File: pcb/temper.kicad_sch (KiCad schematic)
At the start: 0 parts

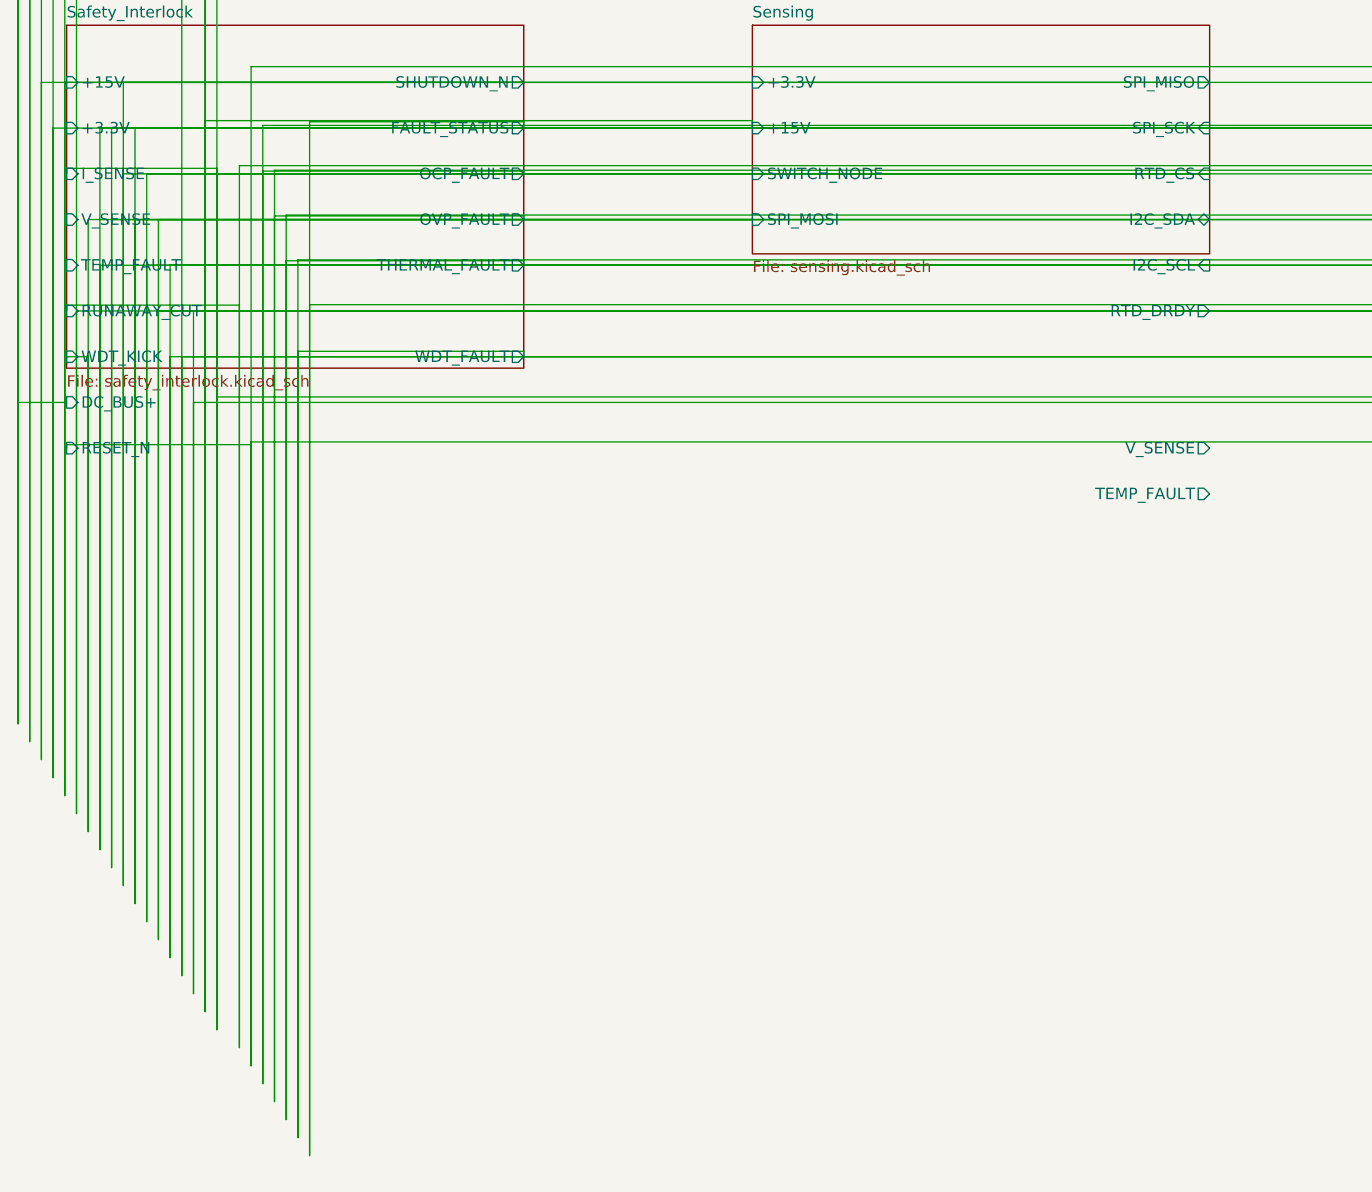
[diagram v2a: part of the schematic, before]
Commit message: fix: close root-vs-child pin reconciliation gaps (NTC_SENSE, stale V_SENSE/TEMP_FAULT/SWITCH_NODE)
Running the full root-vs-child sheet-pin reconciliation the plan promised
but hadn't actually executed found three more instances of the same defect
class the plan was closing out:

- Safety_Interlock's root symbol had V_SENSE/TEMP_FAULT input pins with no
  matching child-side hierarchical label (stale, same class as MCU_ENABLE).
- Safety_Interlock's child sheet declares a real NTC_SENSE input (feeds
  ThermalComparator.ntc_sense directly into the comparator) with no root
  pin at all -- unreachable from outside the sheet. Traced the intended
  source to Sensing, whose own NTC_SENSE producer fed an incomplete
  divider: the pull-up resistor was real, but the actual NTC thermistor
  (NCU18XH103F6SRB, IGBT case temp) was only ever a text annotation, never
  a placed component. Sensing's own V_SENSE/TEMP_FAULT output pins turned
  out to be equally vestigial (no consumer anywhere, never wired) and were
  removed too.
- Sensing's root symbol had a stale SWITCH_NODE input pin with no matching
  child-side label (Half_Bridge has the sheet's one legitimate instance).

Placed the real NTC thermistor and completed its divider in
sensing.kicad_sch, removed all four stale pins, and wired the two missing
NTC_SENSE root pins end to end. Verified via union-find including the full
divider chain and the root-level net.

Co-Authored-By: Claude Sonnet 5 <noreply@anthropic.com>
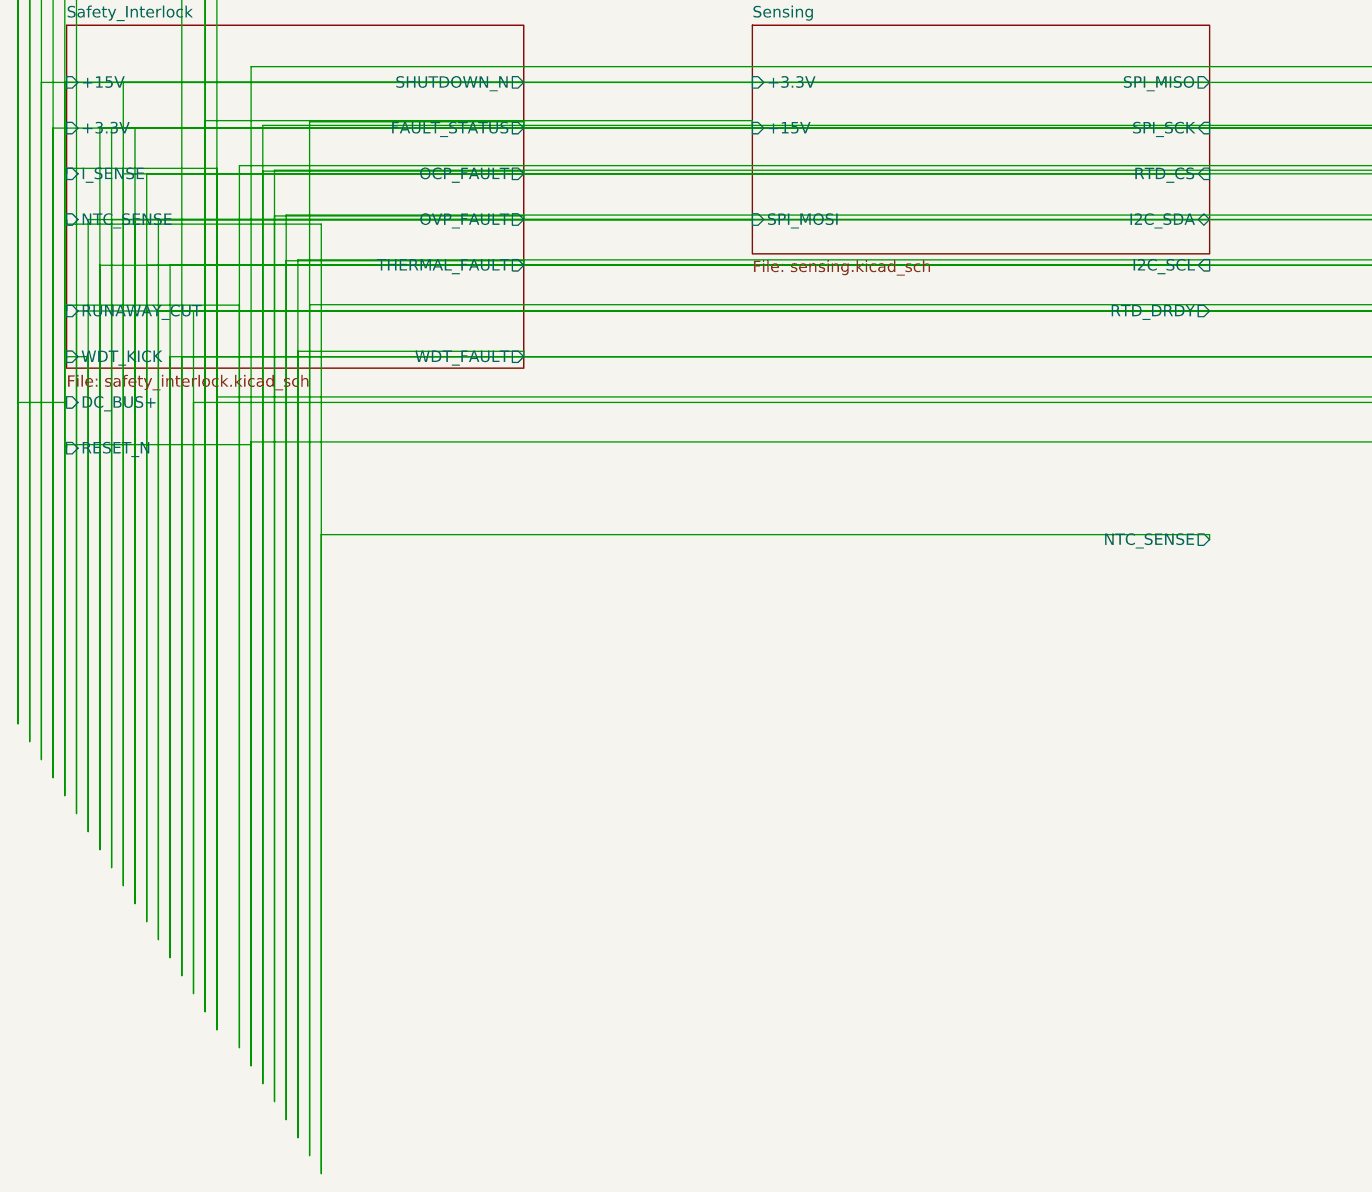
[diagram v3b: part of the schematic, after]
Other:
- sheet Safety_Interlock ports: added NTC_SENSE; removed TEMP_FAULT, V_SENSE
- sheet Sensing ports: added NTC_SENSE; removed SWITCH_NODE, TEMP_FAULT, V_SENSE
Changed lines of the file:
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@@
       )
     )
-    (pin "V_SENSE" input
+    (pin "NTC_SENSE" input
       (at 25.4 173.99 180)
-      (effects
-        (font
-          (size 1.27 1.27)
-        )
-        (justify left)
-      )
-    )
-    (pin "TEMP_FAULT" input
-      (at 25.4 179.07 180)
       (effects
         (font
@@
       )
     )
-    (pin "SWITCH_NODE" input
-      (at 101.6 168.91 180)
-      (effects
-        (font
-          (size 1.27 1.27)
-        )
-        (justify left)
+    (pin "NTC_SENSE" output
+      (at 152.4 209.55 0)
+      (effects
+        (font
+          (size 1.27 1.27)
+        )
+        (justify right)
       )
     )
@@
     (pin "RTD_DRDY" output
       (at 152.4 184.15 0)
-      (effects
-        (font
-          (size 1.27 1.27)
-        )
-        (justify right)
-      )
-    )
-    (pin "V_SENSE" output
-      (at 152.4 199.39 0)
-      (effects
-        (font
-          (size 1.27 1.27)
-        )
-        (justify right)
-      )
-    )
-    (pin "TEMP_FAULT" output
-      (at 152.4 204.47 0)
       (effects
         (font
@@
   (wire (pts (xy 254 183.45) (xy 52.4 183.45)) (stroke (width 0) (type default)))
   (wire (pts (xy 52.4 183.45) (xy 52.4 278.0)) (stroke (width 0) (type default)))
+  (wire (pts (xy 152.4 209.55) (xy 152.4 209.0)) (stroke (width 0) (type default)))
+  (wire (pts (xy 152.4 209.0) (xy 53.7 209.0)) (stroke (width 0) (type default)))
+  (wire (pts (xy 53.7 209.0) (xy 53.7 280.0)) (stroke (width 0) (type default)))
+  (wire (pts (xy 25.4 173.99) (xy 25.4 174.5)) (stroke (width 0) (type default)))
+  (wire (pts (xy 25.4 174.5) (xy 53.7 174.5)) (stroke (width 0) (type default)))
+  (wire (pts (xy 53.7 174.5) (xy 53.7 280.0)) (stroke (width 0) (type default)))
 )
